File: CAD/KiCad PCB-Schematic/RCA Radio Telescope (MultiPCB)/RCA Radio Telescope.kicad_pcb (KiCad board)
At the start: 2 copper layers, 135.2 x 44.8 mm, 52 parts, among them J1 5V In For Filter Board, J11 Conn_01x04_MountingPin, J2 9-12V From PoE Splitter, J3 3V Out For LNA, J4 5V Out For Filter Board, J5 Input from SDR, J7 USB_A, J8 USB_A, Q1 DMP4047LFDE-7, U13 MAX8510EXK30T, U14 TPS62133RGTR, U5 SN74AVC2T45DCUR, U6 MIC5365-1.8YC5-TR, U7 MIC5365-3.3YC5-TR

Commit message: Added KiKit Board Designators to PCB editor and Library
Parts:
- FC, PD: value Board -> Kikit_Board_Label; footprint PCM_kikit:Board -> Library:Kikit_Board_Label
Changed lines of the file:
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@@
 		)
 	)
-	(footprint "PCM_kikit:Board"
+	(footprint "Library:Kikit_Board_Label"
 		(layer "F.Cu")
 		(at 38.6 24.6)
@@
 			)
 		)
-		(property "Value" "Board"
-			(at -7.25 -5 0)
+		(property "Value" "Kikit_Board_Label"
+			(at -11.6 -5.1 0)
 			(layer "Dwgs.User")
 			(effects
@@
 			)
 		)
-		(property "Footprint" "PCM_kikit:Board"
+		(property "Footprint" "Library:Kikit_Board_Label"
 			(at 0 0 0)
 			(layer "F.Fab")
@@
 		)
 	)
-	(footprint "PCM_kikit:Board"
+	(footprint "Library:Kikit_Board_Label"
 		(layer "F.Cu")
 		(at 133.4 19.7)
@@
 			)
 		)
-		(property "Value" "Board"
-			(at -7.25 -5 0)
+		(property "Value" "Kikit_Board_Label"
+			(at -11.5 -5 0)
 			(layer "Dwgs.User")
 			(effects
@@
 			)
 		)
-		(property "Footprint" "PCM_kikit:Board"
+		(property "Footprint" "Library:Kikit_Board_Label"
 			(at 0 0 0)
 			(layer "F.Fab")
@@
 		)
 		(property "Value" "Input from SDR"
-			(at 9.525 1.115 360)
+			(at 9.525 1.115 0)
 			(layer "F.Fab")
 			(effects
@@
 		)
 		(property "Footprint" "Library:PHOENIX_1729144"
-			(at 0 0 360)
+			(at 0 0 0)
 			(layer "F.Fab")
 			(hide yes)
@@
 		)
 		(property "Datasheet" ""
-			(at 0 0 360)
+			(at 0 0 0)
 			(layer "F.Fab")
 			(hide yes)
@@
 		)
 		(property "Description" "Generic screw terminal, single row, 01x04, script generated (kicad-library-utils/schlib/autogen/connector/)"
-			(at 0 0 360)
+			(at 0 0 0)
 			(layer "F.Fab")
 			(hide yes)
@@
 		)
 		(property "Value" "MIC5365-3.3YC5-TR"
-			(at 4.7024 1.8064 360)
+			(at 4.7024 1.8064 0)
 			(layer "F.Fab")
 			(effects
@@
 		)
 		(property "Footprint" "Library:SOT65P210X110-5N"
-			(at 0 0 360)
+			(at 0 0 0)
 			(layer "F.Fab")
 			(hide yes)
@@
 		)
 		(property "Datasheet" ""
-			(at 0 0 360)
+			(at 0 0 0)
 			(layer "F.Fab")
 			(hide yes)
@@
 		)
 		(property "Description" ""
-			(at 0 0 360)
+			(at 0 0 0)
 			(layer "F.Fab")
 			(hide yes)
@@
 		(tags "test point SMD pad")
 		(property "Reference" "TP13"
-			(at 0.025 -2.55 270)
+			(at 0.025 -2.55 -90)
 			(layer "F.SilkS")
 			(effects
@@
 		)
 		(property "Value" "MIC5365-1.8YC5-TR"
-			(at 4.7024 1.8064 360)
+			(at 4.7024 1.8064 0)
 			(layer "F.Fab")
 			(effects
@@
 		)
 		(property "Footprint" "Library:SOT65P210X110-5N"
-			(at 0 0 360)
+			(at 0 0 0)
 			(layer "F.Fab")
 			(hide yes)
@@
 		)
 		(property "Datasheet" ""
-			(at 0 0 360)
+			(at 0 0 0)
 			(layer "F.Fab")
 			(hide yes)
@@
 		)
 		(property "Description" ""
-			(at 0 0 360)
+			(at 0 0 0)
 			(layer "F.Fab")
 			(hide yes)
@@
 		)
 		(fp_text user "${REFERENCE}"
-			(at 0 -3.81 360)
+			(at 0 -3.81 0)
 			(layer "B.Fab")
 			(effects

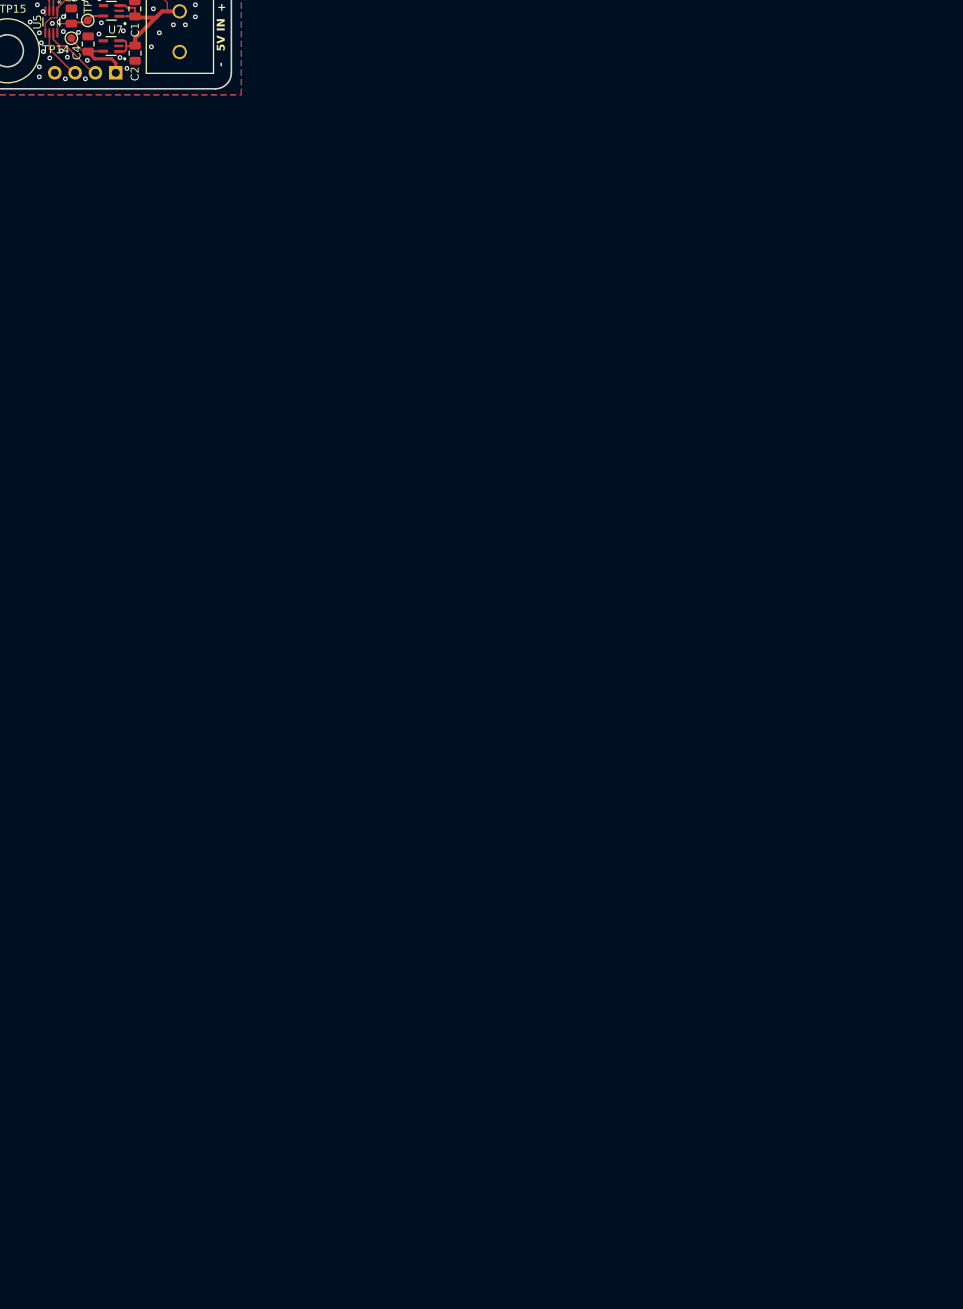
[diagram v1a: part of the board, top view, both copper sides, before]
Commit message: Update to Schematic and PCB
Filter Control Schematic to v1.5
- Removed redundant connector symbol

Root Schematic to v1.9
- Adjusted pin connections for J14 and J14

Created Matching Network PCB
- Filter Board Schematic renamed to MatchNetwork
- Placed RF switches, traces, holes for daughter board, and ground stitching
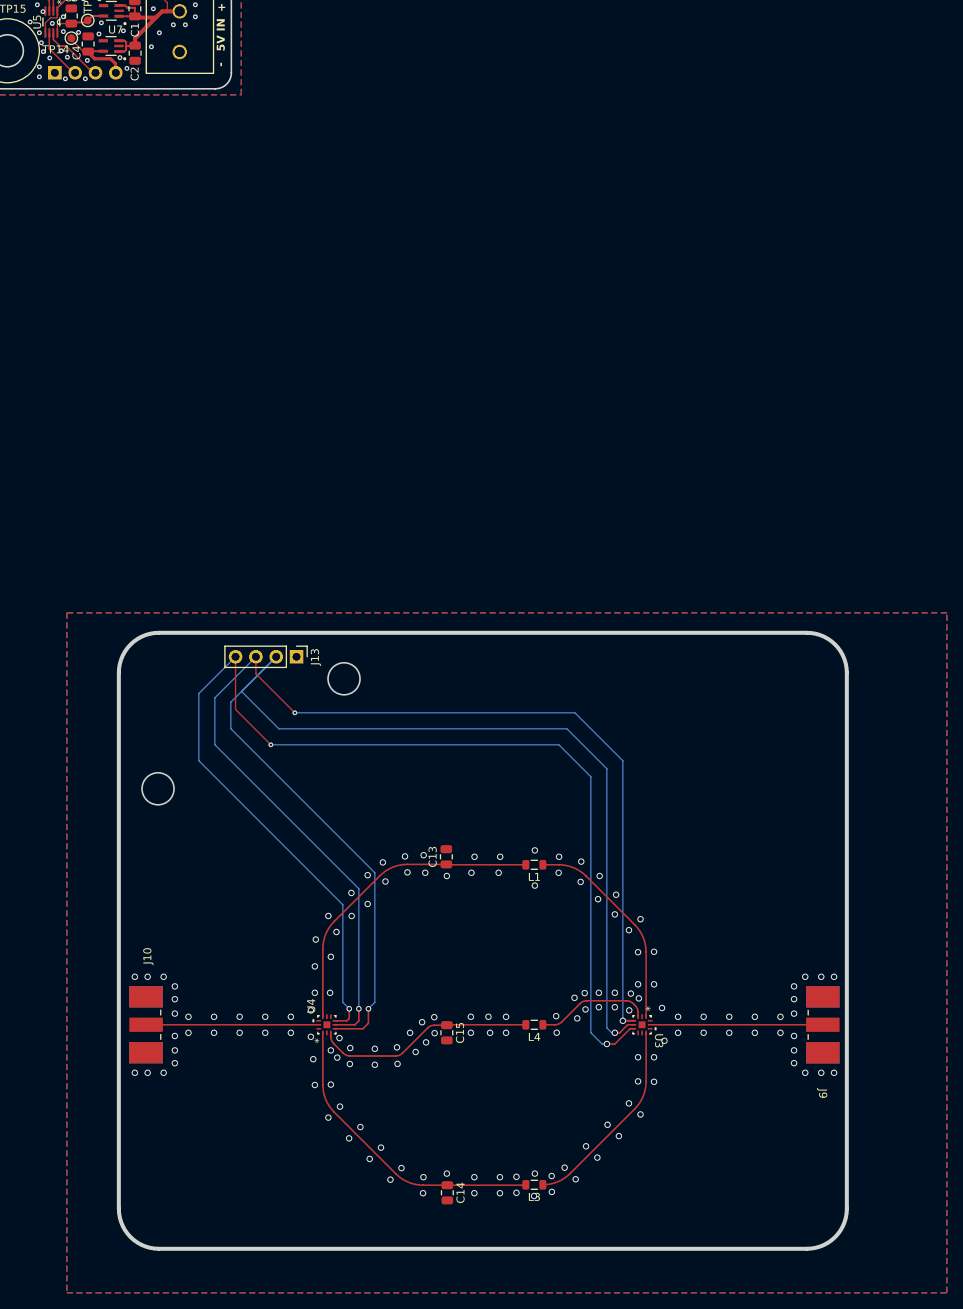
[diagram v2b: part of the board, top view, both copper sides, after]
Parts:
- added C13: C, Capacitor_SMD:C_0805_2012Metric, F.Cu at (189.9, 139.0)
- added C14: C, Capacitor_SMD:C_0805_2012Metric, F.Cu at (190.1, 181.0)
- added C15: C, Capacitor_SMD:C_0805_2012Metric, F.Cu at (190.0, 161.0)
- added FB: Kikit_Board_Label, Library:Kikit_Board_Label, F.Cu at (157.0, 111.0)
- added J10: FILTER_OUT, Library:CONN_142-0711-821_CIN, F.Cu at (147.4, 160.0)
- added J13: Screw_Terminal_01x04, Connector_PinHeader_2.54mm:PinHeader_1x04_P2.54mm_Vertical, F.Cu at (171.2, 114.0)
- added J9: ANT, Library:CONN_142-0711-821_CIN, F.Cu at (242.0, 160.0)
- added L1: L, Inductor_SMD:L_0805_2012Metric, F.Cu at (200.9, 140.0)
- added L3: L, Inductor_SMD:L_0805_2012Metric, F.Cu at (200.9, 180.0)
- added L4: L, Inductor_SMD:L_0805_2012Metric, F.Cu at (200.9, 160.0)
- added U3: SKY13588-460LF, Library:QFN12_SKY, F.Cu at (214.4, 160.0)
- added U4: SKY13588-460LF, Library:QFN12_SKY, F.Cu at (175.0, 160.0)
- J11: value Conn_01x04_MountingPin -> Screw_Terminal_01x04
- TP12: value TestPoint -> FCTRL_VIN
- TP13: value TestPoint -> FCTRL_1V8
- TP14: value TestPoint -> FCTRL_3V3
- TP15: value TestPoint -> FCTRL_GND
- moved J11 7.61 mm to (141.0, 41.0), turned to -90 degrees
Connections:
- C1 pad 2: /FILTER_GND -> /FILTERCTRL_GND
- C2 pad 2: /FILTER_GND -> /FILTERCTRL_GND
- C3 pad 1: /FILTER_GND -> /FILTERCTRL_GND
- C4 pad 1: /FILTER_GND -> /FILTERCTRL_GND
- C4 pad 2: /Filters/+3V3 -> /FiltersCTRL/+3V3
- J1 pad 2: /FILTER_GND -> /FILTERCTRL_GND
- J11 pad 1: /Filters/+3V3 -> /FILTERCTRL_GND
- J11 pad 2: /Filters/INT_CTRL_V1 -> /FiltersCTRL/VSEL_2
- J11 pad 3: /Filters/INT_CTRL_V2 -> /FiltersCTRL/VSEL_1
- J11 pad 4: /FILTER_GND -> /FiltersCTRL/+3V3
- J5 pad 4: /FILTER_GND -> /FILTERCTRL_GND
- TP14 pad 1: /Filters/+3V3 -> /FiltersCTRL/+3V3
- TP15 pad 1: /FILTER_GND -> /FILTERCTRL_GND
- U5 pad 4: /FILTER_GND -> /FILTERCTRL_GND
- U5 pad 6: /Filters/INT_CTRL_V2 -> /FiltersCTRL/VSEL_2
- U5 pad 7: /Filters/INT_CTRL_V1 -> /FiltersCTRL/VSEL_1
- U6 pad 2: /FILTER_GND -> /FILTERCTRL_GND
- U7 pad 2: /FILTER_GND -> /FILTERCTRL_GND
- U7 pad 5: /Filters/+3V3 -> /FiltersCTRL/+3V3
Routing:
- net /MatchNetwork/INT_CTRL_V2: track 0.00 -> 152.7 mm, vias 0 -> 2
- net /MatchNetwork/+3V3: track 0.00 -> 150.0 mm, vias 0 -> 3
- net /MatchNetwork/INT_CTRL_V1: track 0.00 -> 144.7 mm, vias 0 -> 3
- net /MatchNetwork/FILTERA_OUT: track 0.00 -> 39.0 mm
- net /MatchNetwork/FILTERB_OUT: track 0.00 -> 37.8 mm
- net /MatchNetwork/FILTERC_OUT: track 0.00 -> 27.5 mm
- net /MatchNetwork/FILTERA_IN: track 0.00 -> 26.2 mm
- net /MatchNetwork/FILTERB_IN: track 0.00 -> 25.0 mm
- net /MatchNetwork/ANT: track 0.00 -> 19.2 mm
- net /MatchNetwork/FILTER_OUT: track 0.00 -> 19.2 mm
- net /MatchNetwork/FILTERC_IN: track 0.00 -> 14.3 mm
- net /Filters/+3V3: track 10.3 -> 0.00 mm
- net /FiltersCTRL/+3V3: track 0.00 -> 10.2 mm
- net /Filters/INT_CTRL_V1: track 7.80 -> 0.00 mm
- net /FiltersCTRL/VSEL_1: track 0.00 -> 7.49 mm
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- added copper zone on B.Cu, net /FILTERCTRL_GND
- added copper zone on F.Cu, net /FILTERCTRL_GND
- added copper zone on B.Cu, net /MN_GND
- added copper zone on F.Cu, net /MN_GND
- removed copper zone on B.Cu, net /FILTER_GND
- removed copper zone on F.Cu, net /FILTER_GND
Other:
- board size 135.2 x 44.8 mm -> 212.1 x 168.2 mm
- board text added: "Matching Network PCB Rev v1.0 4/3/2025"

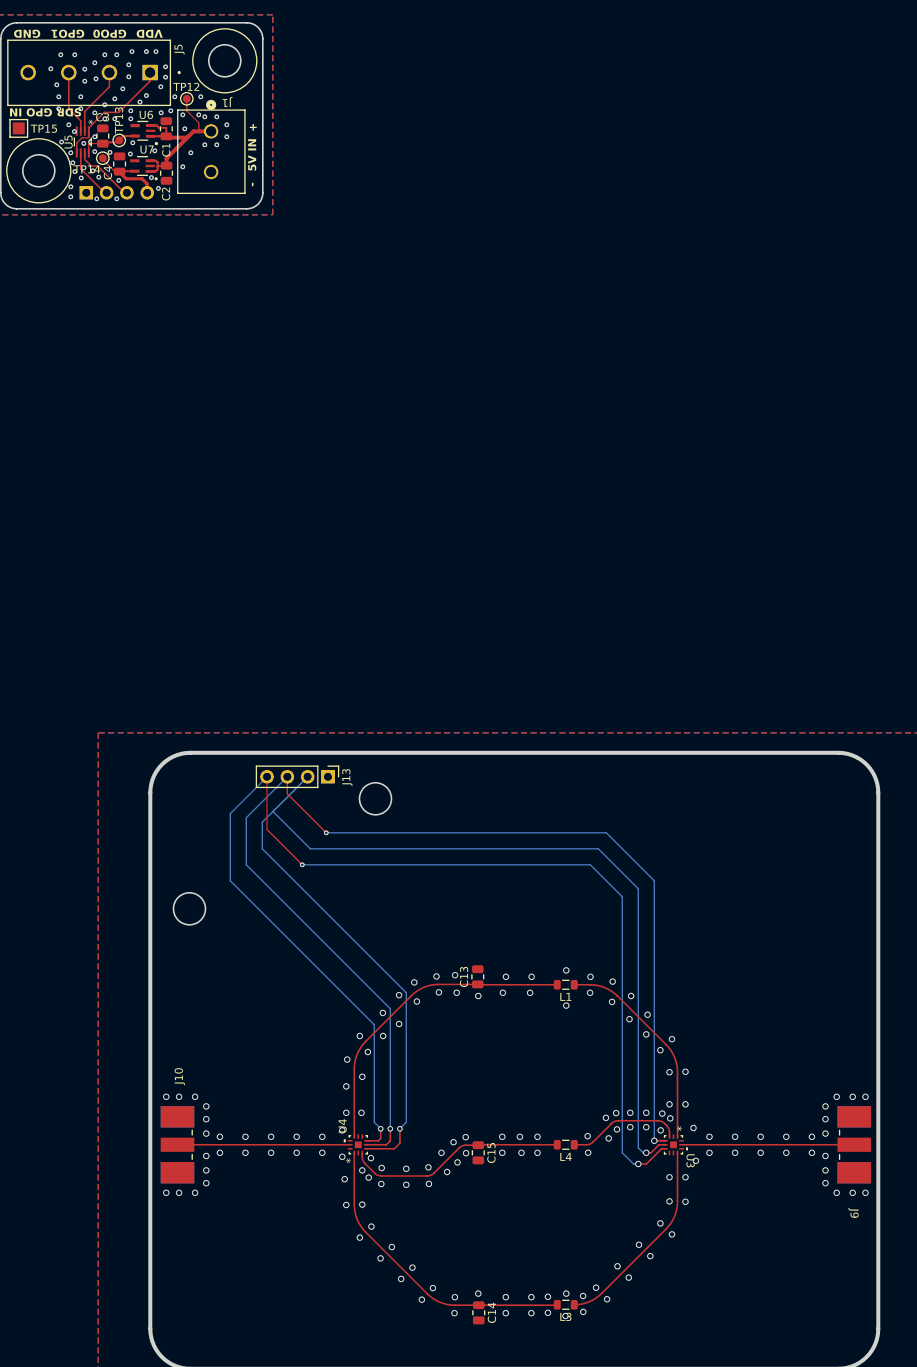
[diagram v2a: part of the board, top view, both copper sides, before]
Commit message: Updated FC board to v1.1
- Removed some vias to reduce required time to solder them
- Adjusted via size to 0.4 to meet EPL specs
-Exported as FC_V1-1 in Kikit exports

Updated Kikit Example
- Added a step guide on how to use tool
- Will make a Git Wiki once done
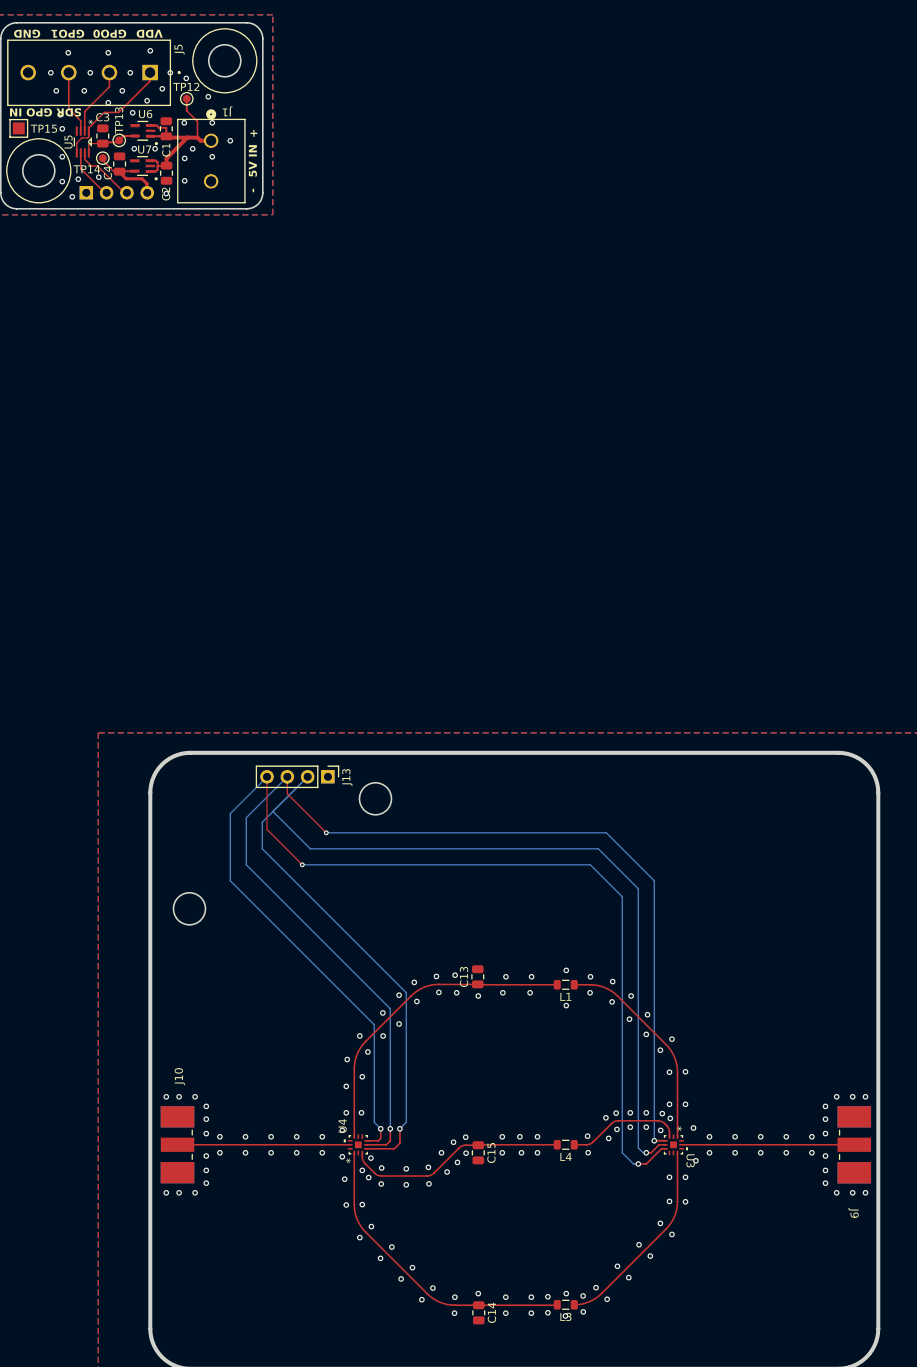
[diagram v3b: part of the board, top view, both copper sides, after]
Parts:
- moved J1 1.17 mm to (156.6, 34.5)
- renumbered FB to MN
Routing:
- net /FiltersCTRL/5V_IN: track 24.7 -> 25.2 mm
- net /FILTERCTRL_GND: vias 70 -> 33
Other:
- board text added: "Filter Control PCB Rev v1.1 4/4/2025"
- board text removed: "Filter Control PCB Rev v1.0 3/30/2025"

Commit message: Updated Schematics and PCBs
Root Schematic to v2.0
- Swapped Matching Network segment for SMD filter
- Updated TODO list

SMD Filter PCB to v1.0
- Added filter and SMA connector footprints
- Imported ADS trace layout
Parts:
- added J11: ANT, Library:CONN_142-0711-821_CIN, F.Cu at (207.2, 101.3)
- added J15: ANT, Library:CONN_142-0711-821_CIN, F.Cu at (360.2, 101.4)
- added U15: BPF-A1340+, RF_Mini-Circuits:Mini-Circuits_HQ1157, F.Cu at (304.3, 101.4)
- moved J13 95.2 mm to (77.2, 129.2)
- moved C13 95.2 mm to (95.9, 154.2)
- moved C14 95.2 mm to (96.1, 196.2)
- moved C15 95.2 mm to (96.0, 176.2)
- moved J10 95.2 mm to (53.4, 175.2)
- moved J9 95.2 mm to (148.0, 175.2)
- moved L1 95.2 mm to (106.9, 155.2)
- moved L3 95.2 mm to (106.9, 195.2)
- moved L4 95.2 mm to (106.9, 175.2)
- moved MN 95.2 mm to (63.0, 126.2)
- moved U3 95.2 mm to (120.4, 175.2)
- moved U4 95.2 mm to (81.0, 175.2)
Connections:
- J10 pad 3: /MN_GND -> (no net)
- J10 pad 4: /MN_GND -> (no net)
- J10 pad 5: /MN_GND -> (no net)
- J10 pad 6: /MN_GND -> (no net)
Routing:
- net /SMDFilter/GND: track 0.00 -> 11.6 mm, vias 0 -> 16
- added copper zone on B.Cu, net /SMDFilter/GND
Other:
- board size 212.1 x 168.2 mm -> 330.1 x 183.4 mm
- board text added: "3.81mm"
- board text added: "SMD Filter PCB Rev v1.0 4/8/2025"
